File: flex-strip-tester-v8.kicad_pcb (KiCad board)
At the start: 2 copper layers, 67.2 x 11.1 mm, 5 parts, among them J1 Conn_01x01_Female, J2 Conn_01x01_Female

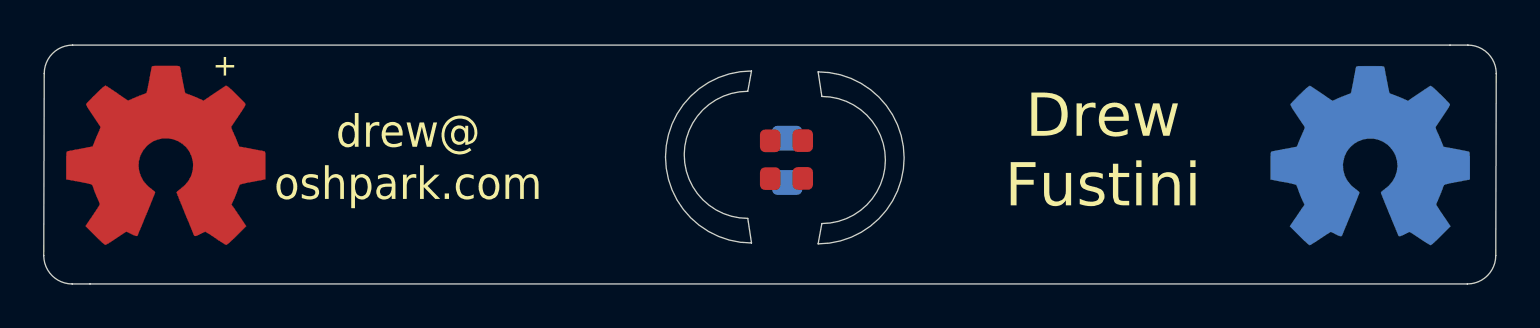
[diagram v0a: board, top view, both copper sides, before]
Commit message: add two LEDs so ligths regardless of polarity
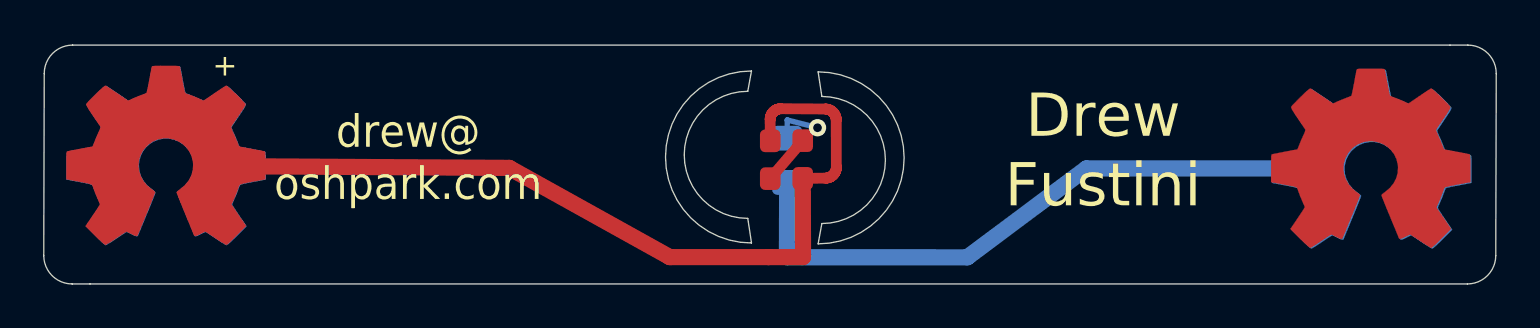
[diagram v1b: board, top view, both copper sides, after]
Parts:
- added J1: Conn_01x01_Female, Symbol:OSHW-Logo2_14.6x12mm_Copper, B.Cu at (124.5, 96.7)
- added J2: Conn_01x01_Female, Symbol:OSHW-Logo2_14.6x12mm_Copper, F.Cu at (180.2, 96.9)
- moved J2 0.17 mm to (180.3, 96.9)
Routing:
- net +3V3: track 0.00 -> 40.4 mm
- net GND: track 0.00 -> 28.8 mm
- net Net-(D1-Pad1): track 0.00 -> 5.52 mm, vias 0 -> 1

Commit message: add v8 of flex tester with two LEDs
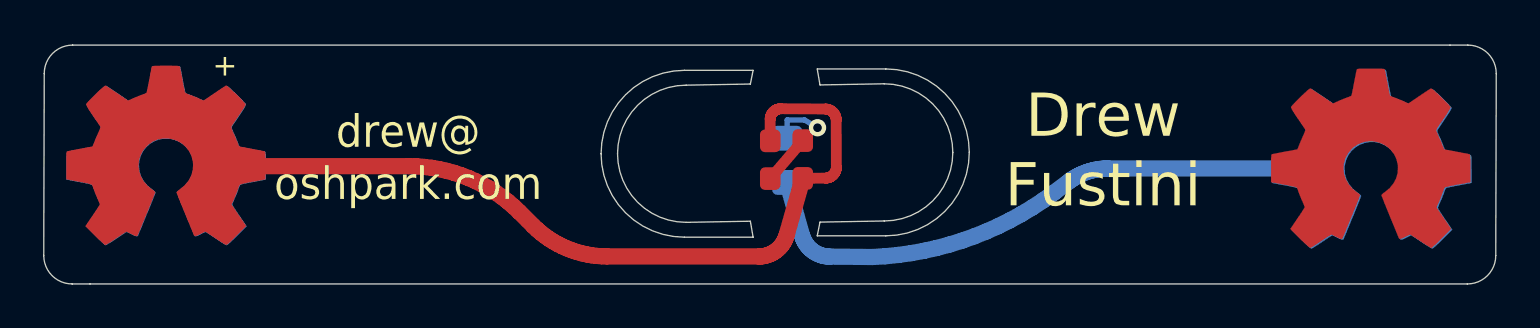
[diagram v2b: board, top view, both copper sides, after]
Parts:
- added J1: Conn_01x01_Female, Symbol:OSHW-Logo2_14.6x12mm_Copper, F.Cu at (124.5, 96.7)
- added J1: Conn_01x01_Female, Symbol:OSHW-Logo2_14.6x12mm_Copper, B.Cu at (124.5, 96.7)
- added J2: Conn_01x01_Female, Symbol:OSHW-Logo2_14.6x12mm_Copper, F.Cu at (180.2, 96.9)
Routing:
- net GND: track 28.8 -> 27.2 mm
- net +3V3: track 40.4 -> 39.2 mm
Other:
- outline, holes or cut-outs redrawn
